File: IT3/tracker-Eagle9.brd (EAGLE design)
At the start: 120 x 89.3 mm, 91 parts, among them J1 THING_PLUS_PHYSICAL, Q1 2N3906, Q2 DMG6602SVT, Q3 DMG6602SVT, Q6 MMBT3906LT1SMD, Q7 DMG6602SVT, U1 ADXL343BCCZ-RL7, U2 FONA-800-BREAKOUTNOHOLE, U3 MP2155GQ-Z, U4 SPARKFUN-SWARM-M138NOTOPHOLE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

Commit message: Update 4V PSUvalues
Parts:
- R10: value 100k -> 121k
- R9: value 820k -> 845k
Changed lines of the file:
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@@
 <attribute name="VOLTAGE_RATING" value="50V" x="-17.399" y="-38.1" size="1.778" layer="27" display="off"/>
 </element>
-<element name="R9" library="SparkFun-Resistors" package="0603" value=" 820k" x="12.954" y="17.78" smashed="yes" rot="R180">
+<element name="R9" library="SparkFun-Resistors" package="0603" value=" 845k" x="12.954" y="17.78" smashed="yes" rot="R180">
 <attribute name="NAME" x="12.954" y="17.018" size="0.889" layer="25" ratio="20" rot="R180" align="bottom-center"/>
 <attribute name="PROD_ID" value=" " x="70.104" y="81.534" size="1.778" layer="27" rot="R180" display="off"/>
@@
 <attribute name="VALUE" x="12.954" y="18.542" size="0.6096" layer="27" font="vector" ratio="20" rot="R180" align="top-center"/>
 </element>
-<element name="R10" library="SparkFun-Resistors" package="0603" value="100k" x="16.256" y="17.78" smashed="yes" rot="R180">
+<element name="R10" library="SparkFun-Resistors" package="0603" value="121k" x="16.256" y="17.78" smashed="yes" rot="R180">
 <attribute name="NAME" x="17.78" y="17.78" size="0.889" layer="25" ratio="20" rot="R180" align="center-right"/>
 <attribute name="PROD_ID" value=" " x="76.708" y="84.836" size="1.778" layer="27" rot="R180" display="off"/>

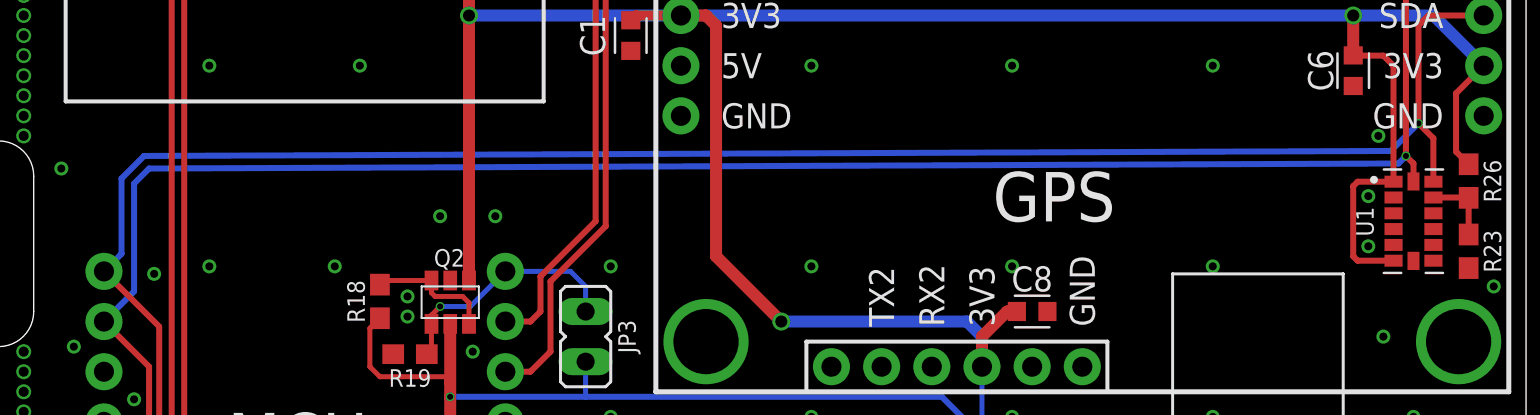
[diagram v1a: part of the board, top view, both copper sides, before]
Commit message: Fixes for accelerometer CS pullup
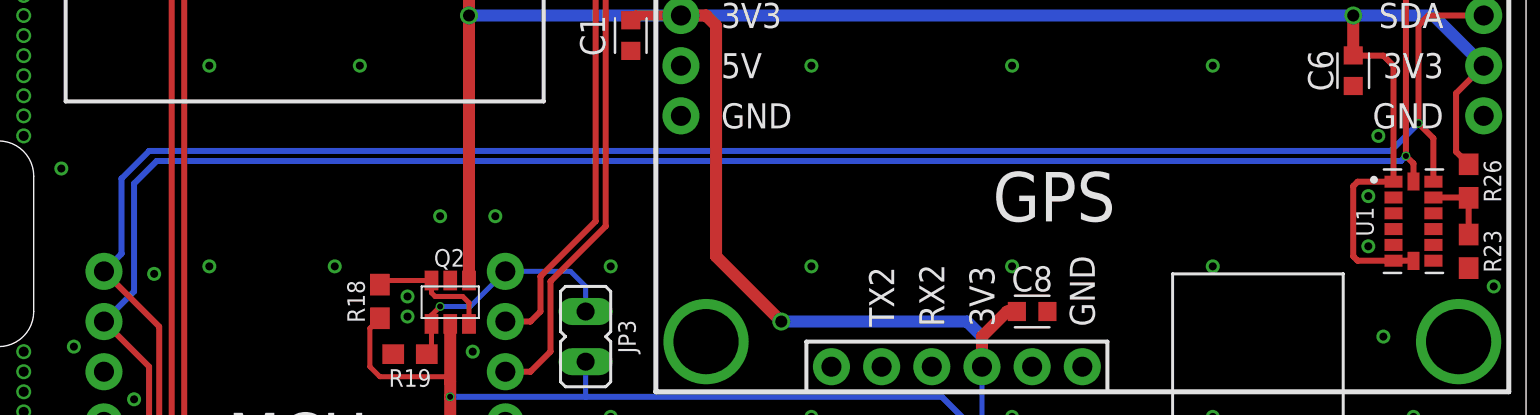
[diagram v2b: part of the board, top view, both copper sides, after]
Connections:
- net V_GPS: now also U1.7
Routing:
- net V_GPS: track 185.8 -> 186.8 mm
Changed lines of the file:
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@@
 <setting verticaltext="up"/>
 </settings>
-<grid distance="0.127" unitdist="mm" unit="mm" style="lines" multiple="1" display="yes" altdistance="0.0127" altunitdist="mm" altunit="mm"/>
+<grid distance="10" unitdist="mil" unit="mil" style="lines" multiple="1" display="yes" altdistance="5" altunitdist="mil" altunit="mil"/>
 <layers>
 <layer number="1" name="Top" color="4" fill="1" visible="yes" active="yes"/>
@@
 <layer number="14" name="Route14" color="22" fill="1" visible="no" active="no"/>
 <layer number="15" name="Route15" color="23" fill="1" visible="no" active="no"/>
-<layer number="16" name="Bottom" color="1" fill="1" visible="no" active="yes"/>
+<layer number="16" name="Bottom" color="1" fill="1" visible="yes" active="yes"/>
 <layer number="17" name="Pads" color="2" fill="1" visible="yes" active="yes"/>
 <layer number="18" name="Vias" color="2" fill="1" visible="yes" active="yes"/>
@@
 <wire x1="50.8" y1="20.574" x2="50.8" y2="49.022" width="0.3048" layer="1"/>
 <wire x1="50.8" y1="49.022" x2="48.006" y2="51.816" width="0.3048" layer="1"/>
-<wire x1="50.038" y1="57.658" x2="113.157" y2="57.912" width="0.3048" layer="16"/>
-<wire x1="113.157" y1="57.912" x2="114.554" y2="59.309" width="0.3048" layer="16"/>
+<wire x1="114.554" y1="59.309" x2="113.157" y2="57.912" width="0.3048" layer="16"/>
 <via x="114.554" y="59.309" extent="1-16" drill="0.3048"/>
 <wire x1="114.554" y1="59.309" x2="114.554" y2="64.262" width="0.3048" layer="1"/>
@@
 <wire x1="115.062" y1="64.77" x2="114.554" y2="64.262" width="0.3048" layer="1"/>
 <contactref element="U1" pad="13"/>
-<wire x1="50.038" y1="57.658" x2="48.895" y2="56.515" width="0.3048" layer="16"/>
 <wire x1="48.895" y1="56.515" x2="48.895" y2="52.705" width="0.3048" layer="16"/>
 <wire x1="48.895" y1="52.705" x2="48.006" y2="51.816" width="0.3048" layer="16"/>
 <wire x1="115.31" y1="56.356" x2="115.31" y2="58.553" width="0.3048" layer="1"/>
 <wire x1="115.31" y1="58.553" x2="114.554" y2="59.309" width="0.3048" layer="1"/>
+<wire x1="113.157" y1="57.912" x2="50.292" y2="57.912" width="0.3048" layer="16"/>
+<wire x1="50.292" y1="57.912" x2="48.895" y2="56.515" width="0.3048" layer="16"/>
 <wire x1="48.006" y1="51.816" x2="77.216" y2="72.39" width="0" layer="19" extent="1-1"/>
 </signal>
@@
 <contactref element="U5" pad="22"/>
 <contactref element="U5" pad="15"/>
-<wire x1="50.292" y1="57.023" x2="49.53" y2="56.261" width="0.3048" layer="16"/>
-<wire x1="49.53" y1="56.261" x2="49.53" y2="50.8" width="0.3048" layer="16"/>
+<wire x1="49.53" y1="50.8" x2="49.53" y2="56.261" width="0.3048" layer="16"/>
 <wire x1="49.53" y1="50.8" x2="48.006" y2="49.276" width="0.3048" layer="16"/>
 <wire x1="53.467" y1="18.669" x2="51.689" y2="18.669" width="0.3048" layer="1"/>
@@
 <wire x1="50.292" y1="20.066" x2="50.292" y2="46.99" width="0.3048" layer="1"/>
 <wire x1="50.292" y1="46.99" x2="48.006" y2="49.276" width="0.3048" layer="1"/>
-<wire x1="50.292" y1="57.023" x2="113.538" y2="57.277" width="0.3048" layer="16"/>
-<wire x1="113.538" y1="57.277" x2="113.919" y2="57.658" width="0.3048" layer="16"/>
+<wire x1="113.665" y1="57.404" x2="113.919" y2="57.658" width="0.3048" layer="16"/>
 <via x="113.919" y="57.658" extent="1-16" drill="0.3048"/>
 <wire x1="113.919" y1="57.658" x2="113.919" y2="66.421" width="0.3048" layer="1"/>
@@
 <wire x1="114.3" y1="56.366" x2="114.3" y2="57.277" width="0.3048" layer="1"/>
 <wire x1="114.3" y1="57.277" x2="113.919" y2="57.658" width="0.3048" layer="1"/>
+<wire x1="49.53" y1="56.261" x2="50.673" y2="57.404" width="0.3048" layer="16"/>
+<wire x1="50.673" y1="57.404" x2="113.665" y2="57.404" width="0.3048" layer="16"/>
 <wire x1="48.006" y1="49.276" x2="77.216" y2="80.01" width="0" layer="19" extent="1-1"/>
 </signal>
@@
 <wire x1="116.459" y1="57.873" x2="116.459" y2="60.833" width="0.3048" layer="1"/>
 <wire x1="116.459" y1="60.833" x2="117.856" y2="62.23" width="0.3048" layer="1"/>
+<contactref element="U1" pad="7"/>
+<wire x1="113.29" y1="52.356" x2="114.29" y2="52.356" width="0.3048" layer="1"/>
+<wire x1="114.29" y1="52.356" x2="114.3" y2="52.346" width="0.3048" layer="1"/>
 </signal>
 <signal name="N$35">
